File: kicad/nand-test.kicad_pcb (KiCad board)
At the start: 2 copper layers, 48.3 x 33 mm, 9 parts, among them J1 PWR, Q1 2N3904, Q2 2N3904, SW1 SW_SPST, SW2 SW_SPST

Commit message: updates gerbers, gcode, and notes
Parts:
- moved J1 10.8 mm to (88.6, 89.2)
- moved R3 10.7 mm to (85.1, 81.8)
- moved R1 10.7 mm to (100.6, 81.8)
- moved R2 10.7 mm to (116.1, 81.8)
- moved Q2 10.6 mm to (123.2, 89.0)
- moved D1 10.4 mm to (104.9, 94.2)
- moved Q1 10.4 mm to (115.3, 89.0)
- moved SW1 9.27 mm to (94.3, 69.1)
- moved SW2 9.27 mm to (109.5, 69.1)
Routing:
- net GND: track 0.11 -> 39.7 mm
- net Net-(Q2-Pad2): track 8.67 -> 10.0 mm
- net Net-(R1-Pad1): track 13.4 -> 14.7 mm
- net Net-(R2-Pad1): track 13.4 -> 14.7 mm
- net Net-(D1-Pad2): track 22.8 -> 24.0 mm
- net +5V: track 46.5 -> 47.1 mm
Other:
- board size 48.3 x 33 mm -> 50 x 33.5 mm

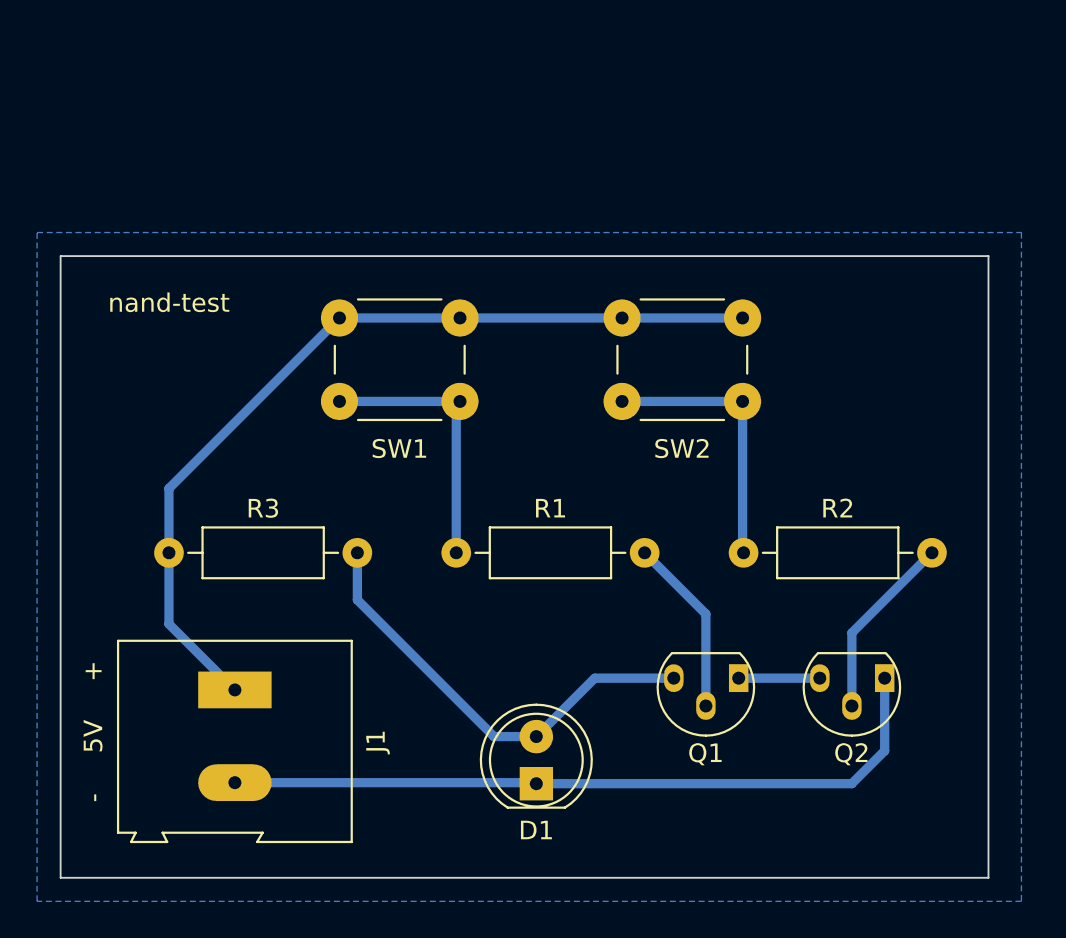
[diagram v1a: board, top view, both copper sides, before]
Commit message: adds silkscreen steps
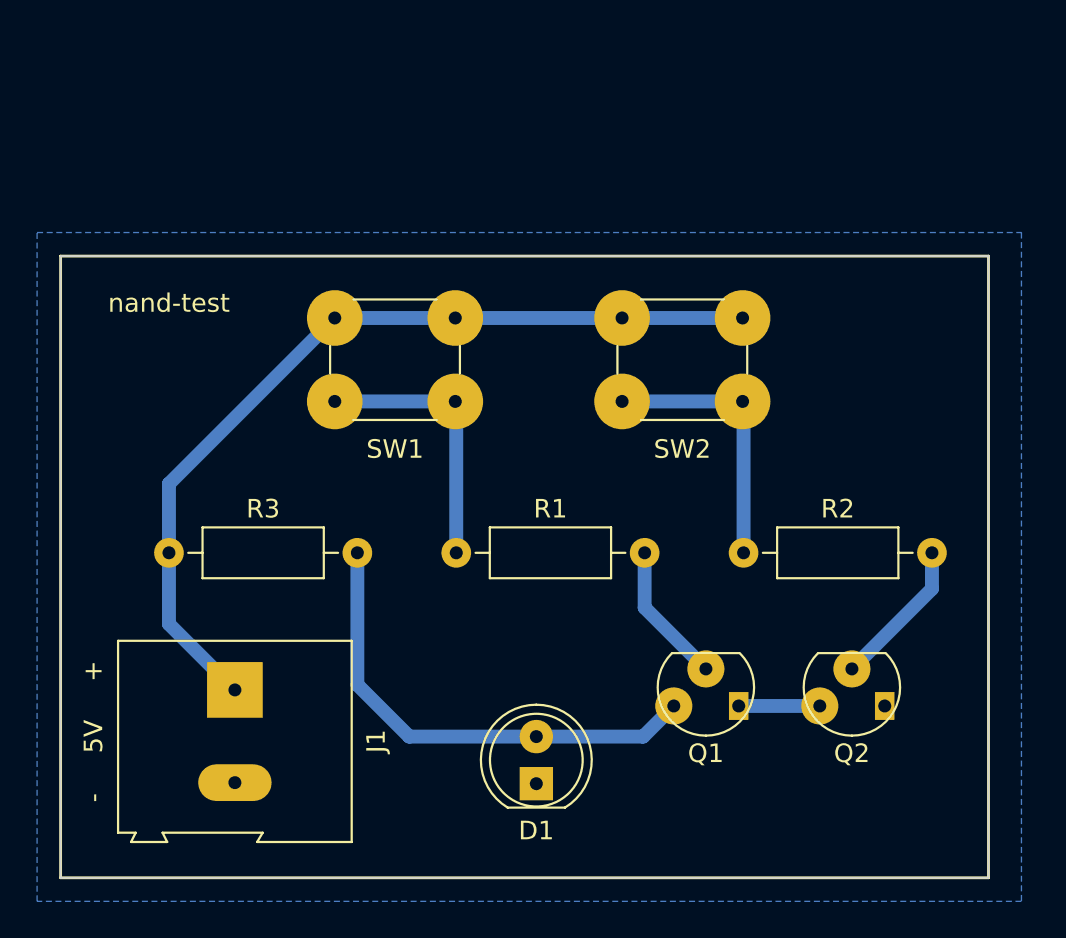
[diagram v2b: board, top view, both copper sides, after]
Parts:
- moved SW1 0.25 mm to (94.0, 69.1)
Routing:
- net GND: track 39.7 -> 0.00 mm
- net Net-(D1-Pad2): track 24.0 -> 26.0 mm
- net Net-(Q2-Pad2): track 10.0 -> 8.05 mm
- net Net-(Q1-Pad2): track 9.63 -> 7.63 mm
